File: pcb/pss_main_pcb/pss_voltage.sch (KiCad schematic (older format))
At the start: 12 parts, among them J1 24V DC Input, J2 220V AC Input, U1 LM2596S-5, U2 LM2596S-3.3

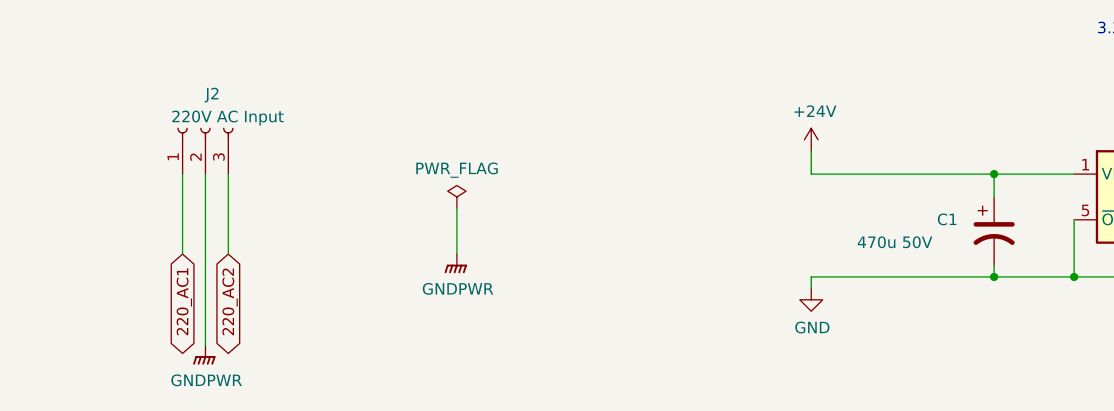
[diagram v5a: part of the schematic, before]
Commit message: Change footprints and place some new components
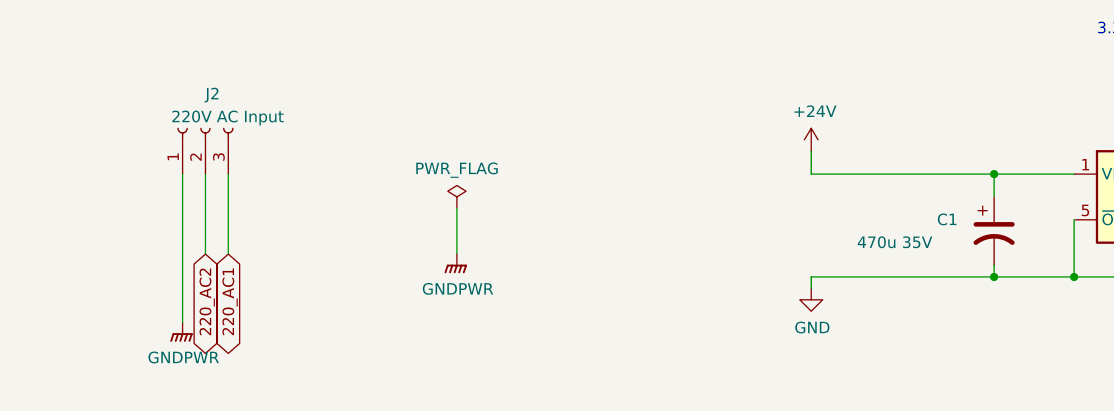
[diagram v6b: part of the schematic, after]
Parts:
- C1: value 470u 50V -> 470u 35V; footprint Capacitor_SMD:CP_Elec_16x17.5 -> Capacitor_SMD:CP_Elec_10x10.5
- J1: footprint Connector_AMASS:AMASS_XT60-F_1x02_P7.20mm_Vertical -> Connector_AMASS:AMASS_XT30U-F_1x02_P5.0mm_Vertical
- J2: footprint Connector:Banana_Jack_3Pin -> Connector_Wire:SolderWire-2.5sqmm_1x03_P7.2mm_D2.4mm_OD3.6mm
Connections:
- net 220_AC1: now also J2.3 (Pin_3); no longer J2.1 (Pin_1)
- net 220_AC2: now also J2.2 (Pin_2); no longer J2.3 (Pin_3)
- net GNDPWR: now also J2.1 (Pin_1); no longer J2.2 (Pin_2)
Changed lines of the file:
@@
 	1    0    0    -1
 $EndComp
-Text GLabel 2550 4650 3    50   BiDi ~ 0
+Text GLabel 2750 4650 3    50   BiDi ~ 0
 220_AC1
 $Comp
@@
 F 0 "J1" V 2450 2150 50  0000 L CNN
 F 1 "24V DC Input" V 2550 2000 50  0000 L CNN
-F 2 "Connector_AMASS:AMASS_XT60-F_1x02_P7.20mm_Vertical" H 2650 2250 50  0001 C CNN
+F 2 "Connector_AMASS:AMASS_XT30U-F_1x02_P5.0mm_Vertical" H 2650 2250 50  0001 C CNN
 F 3 "~" H 2650 2250 50  0001 C CNN
 	1    2650 2250
@@
 AR Path="/5ED9AD16/5EDEFDBB" Ref="C1"  Part="1"
 F 0 "C1" H 5850 4600 50  0000 L CNN
-F 1 "470u 50V" H 5500 4500 50  0000 L CNN
-F 2 "Capacitor_SMD:CP_Elec_16x17.5" H 6100 4550 50  0001 C CNN
+F 1 "470u 35V" H 5500 4500 50  0000 L CNN
+F 2 "Capacitor_SMD:CP_Elec_10x10.5" H 6100 4550 50  0001 C CNN
 F 3 "~" H 6100 4550 50  0001 C CNN
 	1    6100 4550
@@
 Wire Wire Line
 	8900 4500 9250 4500
-Wire Wire Line
-	2550 4300 2550 4650
 $Comp
 L power:PWR_FLAG #FLG02
@@
 F 0 "J2" V 2800 4100 50  0000 R CNN
 F 1 "220V AC Input" V 2700 4250 50  0000 R CNN
-F 2 "Connector:Banana_Jack_3Pin" H 2650 4100 50  0001 C CNN
+F 2 "Connector_Wire:SolderWire-2.5sqmm_1x03_P7.2mm_D2.4mm_OD3.6mm" H 2650 4100 50  0001 C CNN
 F 3 "~" H 2650 4100 50  0001 C CNN
 	1    2650 4100
 	0    -1   -1   0
 $EndComp
-Text GLabel 2750 4650 3    50   BiDi ~ 0
+Text GLabel 2650 4650 3    50   BiDi ~ 0
 220_AC2
 Wire Wire Line
@@
 L power:GNDPWR #PWR03
 U 1 1 5ECE62C4
-P 2650 5050
-F 0 "#PWR03" H 2650 4850 50  0001 C CNN
-F 1 "GNDPWR" H 2654 4896 50  0000 C CNN
-F 2 "" H 2650 5000 50  0001 C CNN
-F 3 "" H 2650 5000 50  0001 C CNN
-	1    2650 5050
-	1    0    0    -1
-$EndComp
-Wire Wire Line
-	2650 5050 2650 4300
+P 2550 4950
+F 0 "#PWR03" H 2550 4750 50  0001 C CNN
+F 1 "GNDPWR" H 2554 4796 50  0000 C CNN
+F 2 "" H 2550 4900 50  0001 C CNN
+F 3 "" H 2550 4900 50  0001 C CNN
+	1    2550 4950
+	1    0    0    -1
+$EndComp
 $Comp
 L power:GNDPWR #PWR?
@@
 Wire Wire Line
 	5300 2850 6950 2850
+Wire Wire Line
+	2550 4300 2550 4950
+Wire Wire Line
+	2650 4650 2650 4300
 $EndSCHEMATC

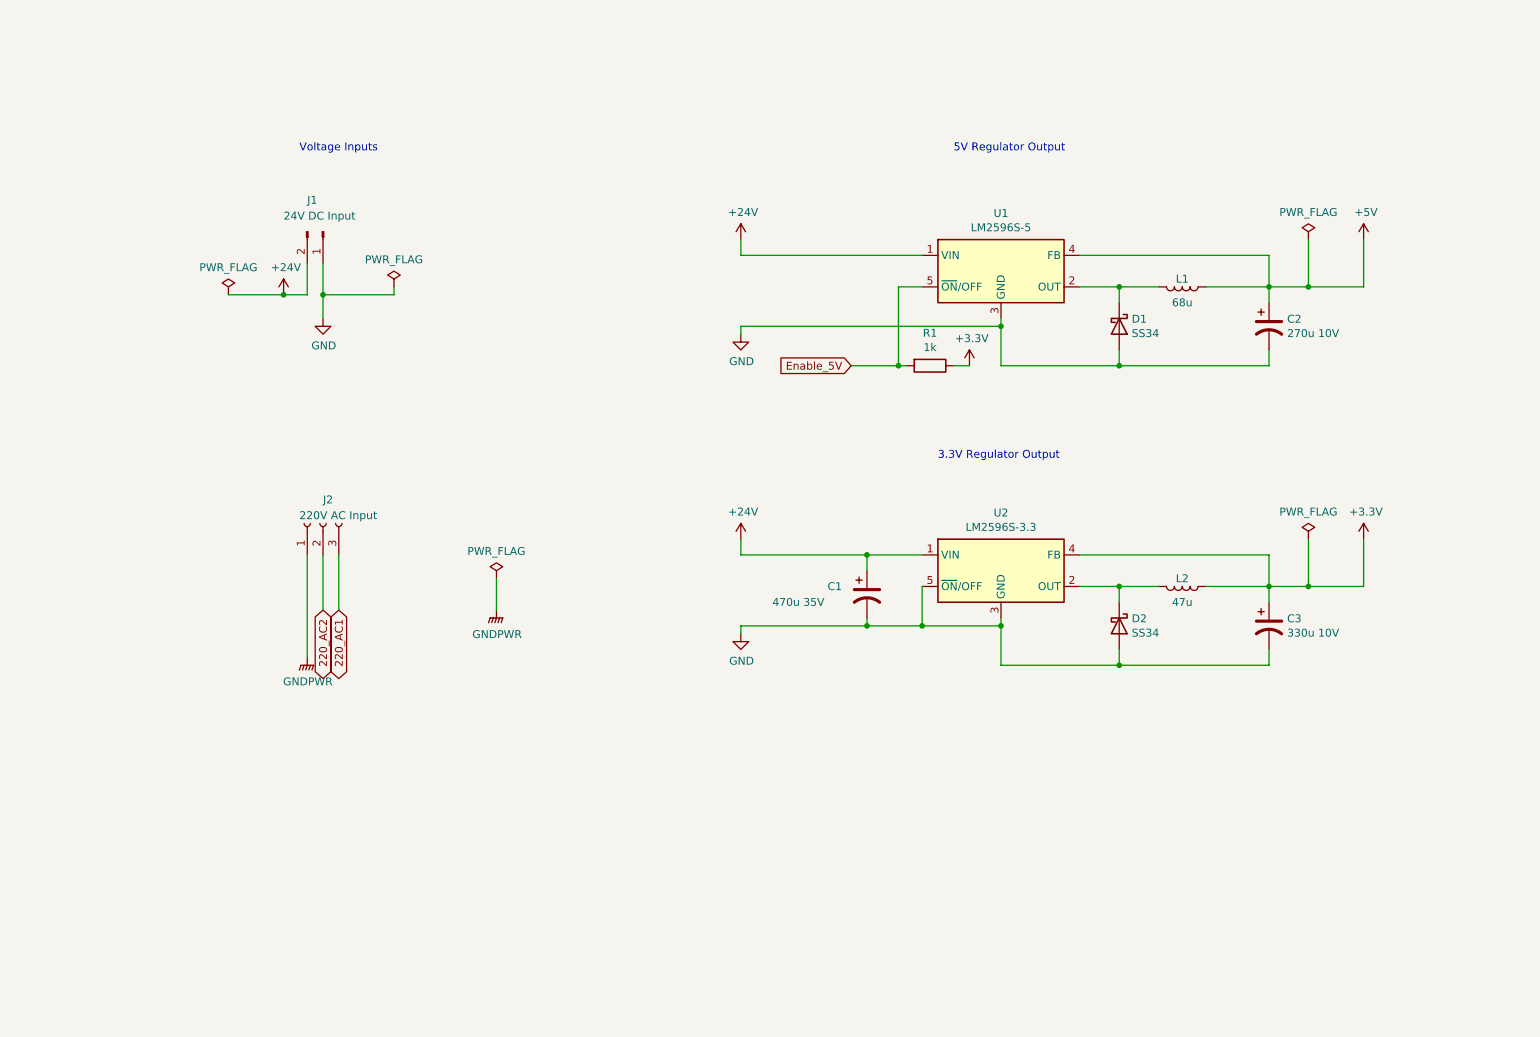
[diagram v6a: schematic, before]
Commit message: Add 3D models and totaly redesign PCB
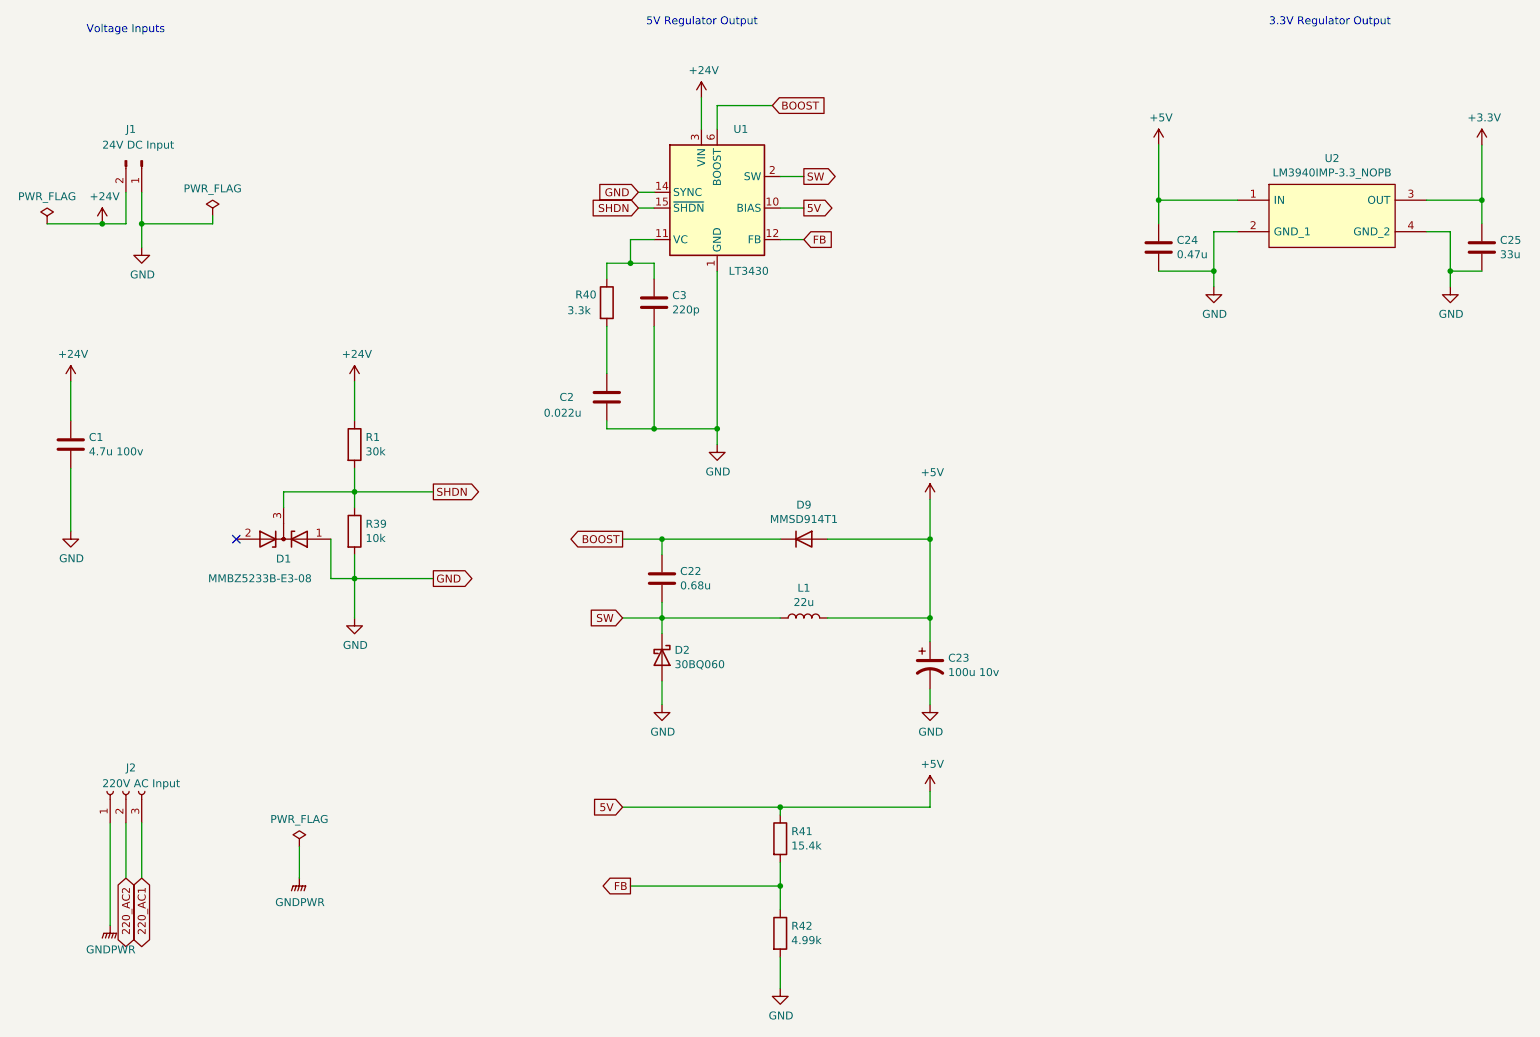
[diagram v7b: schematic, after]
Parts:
- removed C1: 470u 35V, Capacitor_SMD:CP_Elec_10x10.5, symbol Device:CP1
- removed C2: 270u 10V, Capacitor_SMD:CP_Elec_8x10.5, symbol Device:CP1
- removed C3: 330u 10V, Capacitor_SMD:CP_Elec_8x10.5, symbol Device:CP1
- removed D1: SS34, Diode_SMD:D_SMA_Handsoldering, symbol Device:D_Schottky
- removed L2: 47u, Inductor_SMD:L_Taiyo-Yuden_NR-30xx_HandSoldering, symbol Device:L
- removed U1: LM2596S-5, Package_TO_SOT_SMD:TO-263-5_TabPin3, symbol Regulator_Switching:LM2596S-5
- removed U2: LM2596S-3.3, Package_TO_SOT_SMD:TO-263-5_TabPin3, symbol Regulator_Switching:LM2596S-3.3
- added C1: 4.7u 100v, Capacitor_SMD:CP_Elec_5x5.4, symbol Device:C
- added C2: 0.022u, Capacitor_SMD:C_1206_3216Metric_Pad1.33x1.80mm_HandSolder, symbol Device:C
- added C22: 0.68u, Capacitor_SMD:C_1206_3216Metric_Pad1.33x1.80mm_HandSolder, symbol Device:C
- added C23: 100u 10v, Capacitor_SMD:CP_Elec_6.3x7.7, symbol Device:CP1
- added C24: 0.47u, Capacitor_SMD:C_1206_3216Metric_Pad1.33x1.80mm_HandSolder, symbol Device:C
- added C25: 33u, Capacitor_SMD:C_1206_3216Metric_Pad1.33x1.80mm_HandSolder, symbol Device:C
- added C3: 220p, Capacitor_SMD:C_1206_3216Metric_Pad1.33x1.80mm_HandSolder, symbol Device:C
- added D1: MMBZ5233B-E3-08, Package_TO_SOT_SMD:SOT-23, symbol Device:D_Zener_x2_KCom_AAK
- added D9: MMSD914T1, Diode_SMD:D_SOD-123, symbol Device:D
- added R39: 10k, Resistor_SMD:R_1206_3216Metric_Pad1.30x1.75mm_HandSolder, symbol Device:R
- added R40: 3.3k, Resistor_SMD:R_1206_3216Metric_Pad1.30x1.75mm_HandSolder, symbol Device:R
- added R41: 15.4k, Resistor_SMD:R_1206_3216Metric_Pad1.30x1.75mm_HandSolder, symbol Device:R
- added R42: 4.99k, Resistor_SMD:R_1206_3216Metric_Pad1.30x1.75mm_HandSolder, symbol Device:R
- added U1: LT3430, Package_SO:TSSOP-14-1EP_4.4x5mm_P0.65mm, symbol Regulator_Switching:LT3430
- added U2: LM3940IMP-3.3_NOPB, Package_TO_SOT_SMD:SOT-223, symbol LM3940IMP-3.3_NOPB:LM3940IMP-3.3_NOPB
- D2: value SS34 -> 30BQ060; footprint Diode_SMD:D_SMA_Handsoldering -> Diode_SMD:D_SMC_Handsoldering
- L1: value 68u -> 22u; footprint Inductor_SMD:L_Taiyo-Yuden_NR-30xx_HandSoldering -> inductors:L_12x12mm_H8mm
- R1: value 1k -> 30k; footprint Resistor_SMD:R_1206_3216Metric_Pad1.42x1.75mm_HandSolder -> Resistor_SMD:R_1206_3216Metric_Pad1.30x1.75mm_HandSolder
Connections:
- net +24V: now also R1.1, C1.1, U1.3 (VIN), U1.4 (VIN)
- net +3V3: now also C25.1, U2.3 (OUT); no longer R1.1
- net +5V: now also L1.2, C23.1, C24.1, D9.2 (A), R41.1, U1.10 (BIAS), U2.1 (IN); no longer L1.1
- net GND: now also C1.2, C2.2, C23.2, C24.2, C25.2, C3.2, D1.1 (A), R39.2, R42.2, U1.1 (GND), U1.14 (SYNC), U1.16 (GND), U1.17 (GND), U1.8 (GND), U1.9 (GND), U2.2 (GND_1), U2.4 (GND_2)
- net SW: now reaches D2.1 (K)
- net SW: now also L1.1, C22.2, U1.2 (SW), U1.5 (SW)
- net Enable_5V renamed SHDN
- net SHDN: now also D1.3 (K), R39.1, U1.15 (~SHDN)
- new net: C3.1, R40.1, U1.11 (VC)
- new net: C2.1, R40.2
- new net BOOST: C22.1, D9.1 (K), U1.6 (BOOST)
- new net FB: R41.2, R42.1, U1.12 (FB)
- no-connect marks 0 -> 1
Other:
- moved on the sheet: J1, J2
